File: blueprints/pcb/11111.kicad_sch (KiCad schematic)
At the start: 128 parts, among them J1 MJ-4PP-9, J2 MJ-4PP-9, SW1 SW_Push, SW10 SW_Push, SW11 SW_Push, SW12 SW_Push, SW13 SW_Push, SW14 SW_Push, SW15 SW_Push, SW16 SW_Push, SW17 SW_Push, SW18 SW_Push, SW19 SW_Push, SW2 SW_Push, SW20 SW_Push, SW21 SW_Push, SW22 SW_Push, SW23 SW_Push, SW24 SW_Push, SW25 SW_Push, SW26 SW_Push, SW27 SW_Push, SW28 SW_Push, SW29 SW_Push, SW3 SW_Push, SW30 SW_Push, SW31 SW_Push, SW32 SW_Push, SW33 SW_Push, SW34 SW_Push, SW35 SW_Push, SW36 SW_Push, SW37 SW_Push, SW38 SW_Push, SW39 SW_Push, SW4 SW_Push, SW40 SW_Push, SW41 SW_Push, SW42 SW_Push, SW43 SW_Push, SW44 SW_Push, SW45 SW_Push, SW46 SW_Push, SW47 SW_Push, SW48 SW_Push, SW49 SW_Push, SW5 SW_Push, SW50 SW_Push, SW51 SW_Push, SW52 SW_Push, SW53 SW_Push, SW54 SW_Push, SW55 SW_Push, SW56 SW_Push, SW57 SW_Push, SW58 SW_Push, SW59 SW_Push, SW6 SW_Push, SW60 SW_Push, SW61 SW_Push, SW62 SW_Push, SW7 SW_Push, SW8 SW_Push, SW9 SW_Push

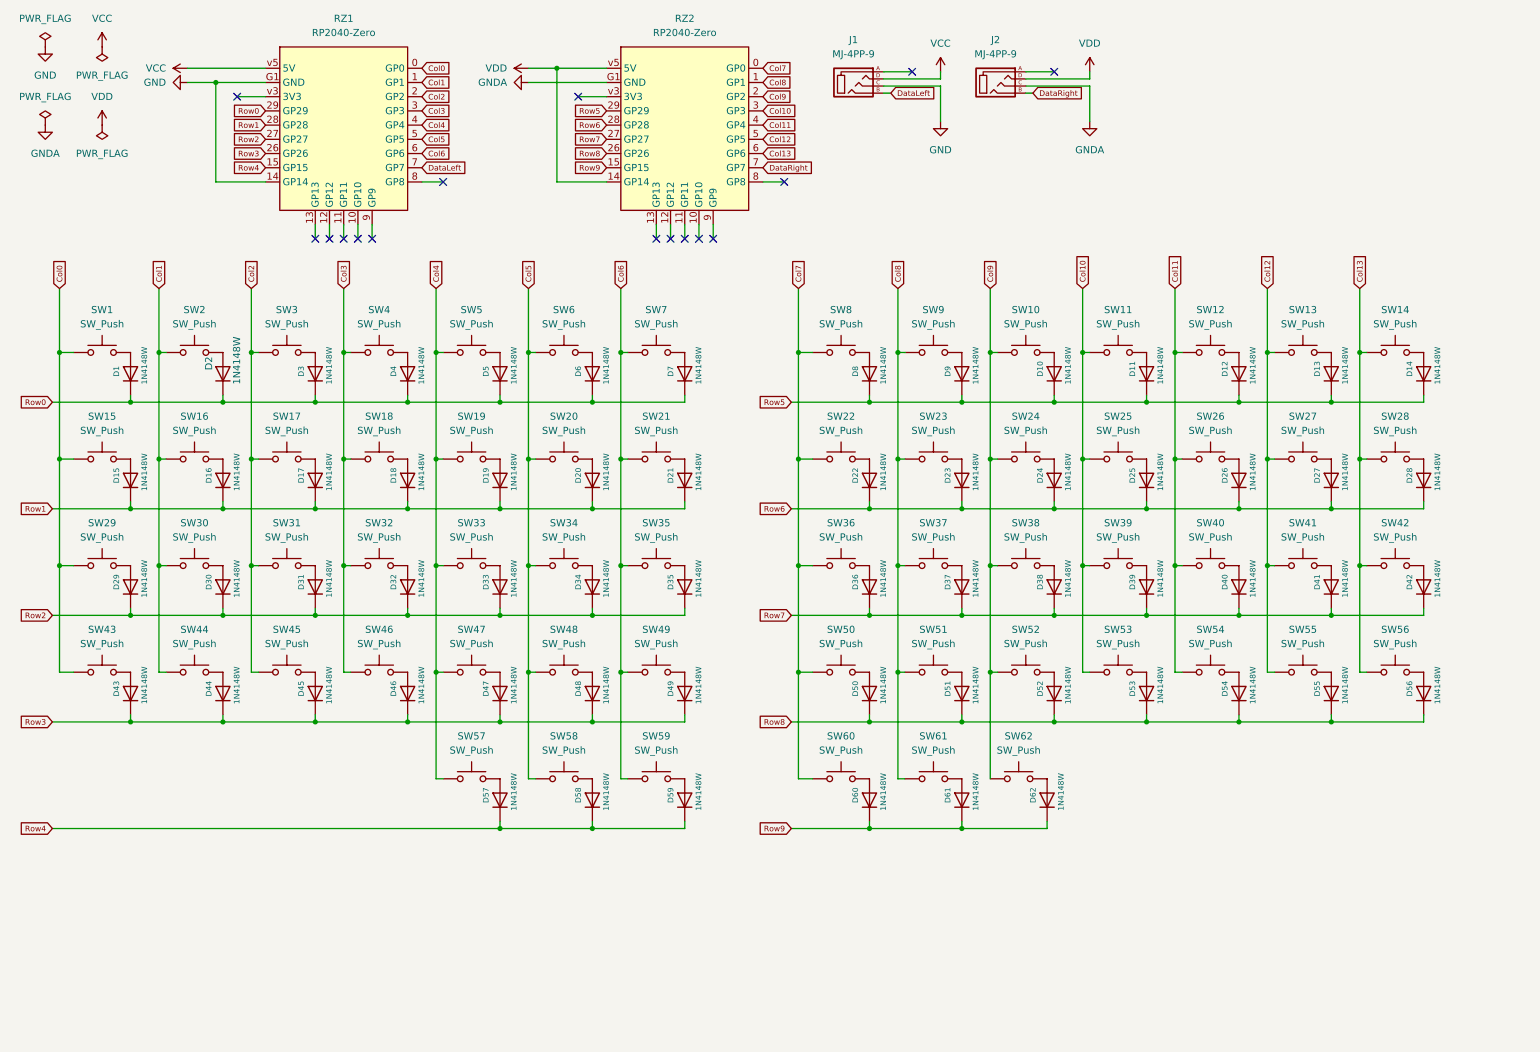
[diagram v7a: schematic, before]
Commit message: update PCB, use Raspberry Pi Pico
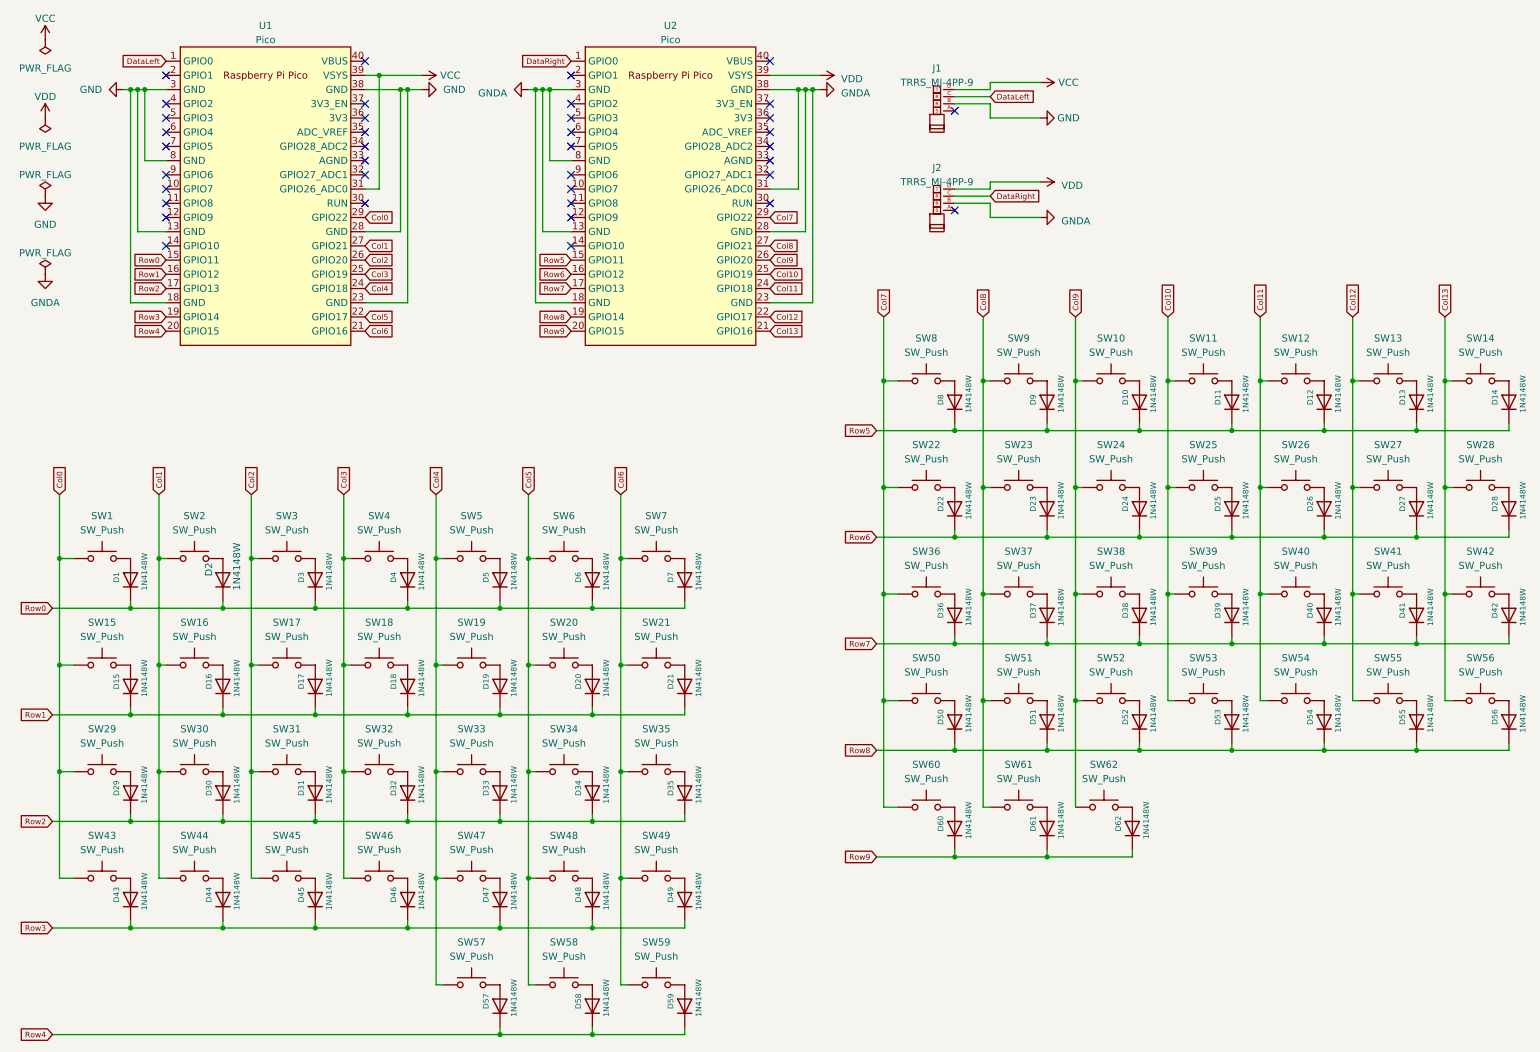
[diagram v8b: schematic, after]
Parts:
- removed J1, J2: MJ-4PP-9, foostan:MJ-4PP-9_1side, symbol foostan_kbd:MJ-4PP-9
- removed RZ1, RZ2: RP2040-Zero, RP2040-zero:rp2040-zero, symbol keyboard_utils:RP2040-Zero
- added J1, J2: TRRS_MJ-4PP-9, Salicylic-acid3_kbd_Parts:TRRS_MJ-4PP-9, symbol Salicylic-acid3_kbd_Parts:TRRS_MJ-4PP-9
- added U1, U2: Pico, Raspberry-pi-pico:RPi_Pico_SMD_TH, symbol raspberry_pi_pico:Pico
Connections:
- net Col0: now also U1.29 (GPIO22)
- net Col1: now also U1.27 (GPIO21)
- net Col10: now also U2.25 (GPIO19)
- net Col11: now also U2.24 (GPIO18)
- net Col12: now also U2.22 (GPIO17)
- net Col13: now also U2.21 (GPIO16)
- net Col2: now also U1.26 (GPIO20)
- net Col3: now also U1.25 (GPIO19)
- net Col4: now also U1.24 (GPIO18)
- net Col5: now also U1.22 (GPIO17)
- net Col6: now also U1.21 (GPIO16)
- net Col7: now also U2.29 (GPIO22)
- net Col8: now also U2.27 (GPIO21)
- net Col9: now also U2.26 (GPIO20)
- net DataLeft: now also J1.C, U1.1 (GPIO0)
- net DataRight: now also J2.C, U2.1 (GPIO0)
- net GND: now also J1.B, U1.13 (GND), U1.18 (GND), U1.23 (GND), U1.28 (GND), U1.3 (GND), U1.38 (GND), U1.8 (GND)
- net GNDA: now also J2.B, U2.13 (GND), U2.18 (GND), U2.23 (GND), U2.28 (GND), U2.3 (GND), U2.31 (GPIO26_ADC0), U2.38 (GND), U2.8 (GND)
- net Row0: now also U1.15 (GPIO11)
- net Row1: now also U1.16 (GPIO12)
- net Row2: now also U1.17 (GPIO13)
- net Row3: now also U1.19 (GPIO14)
- net Row4: now also U1.20 (GPIO15)
- net Row5: now also U2.15 (GPIO11)
- net Row6: now also U2.16 (GPIO12)
- net Row7: now also U2.17 (GPIO13)
- net Row8: now also U2.19 (GPIO14)
- net Row9: now also U2.20 (GPIO15)
- net VCC: now also J1.D, U1.31 (GPIO26_ADC0), U1.39 (VSYS)
- net VDD: now also J2.D, U2.39 (VSYS)
- no-connect marks 16 -> 38
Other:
- moved on the sheet: D1, D10, D11, D12, D13, D14, D15, D16, D17, D18, D19, D2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
